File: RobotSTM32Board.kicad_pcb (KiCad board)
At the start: 2 copper layers, 70 x 82.5 mm, 19 parts, among them IC1 TB6612FNG, IC2 TB6612FNG, J1 MotorA, J2 MotorB, J3 MotorC, J4 MotorD, J5 EncoderA, J6 EncoderB, J7 EncoderC, J8 EncoderD, J9 ESTOP, U1 NUCLEO-F410RB, U2 BNO085, U3 ESP32-S3-WROOM-1

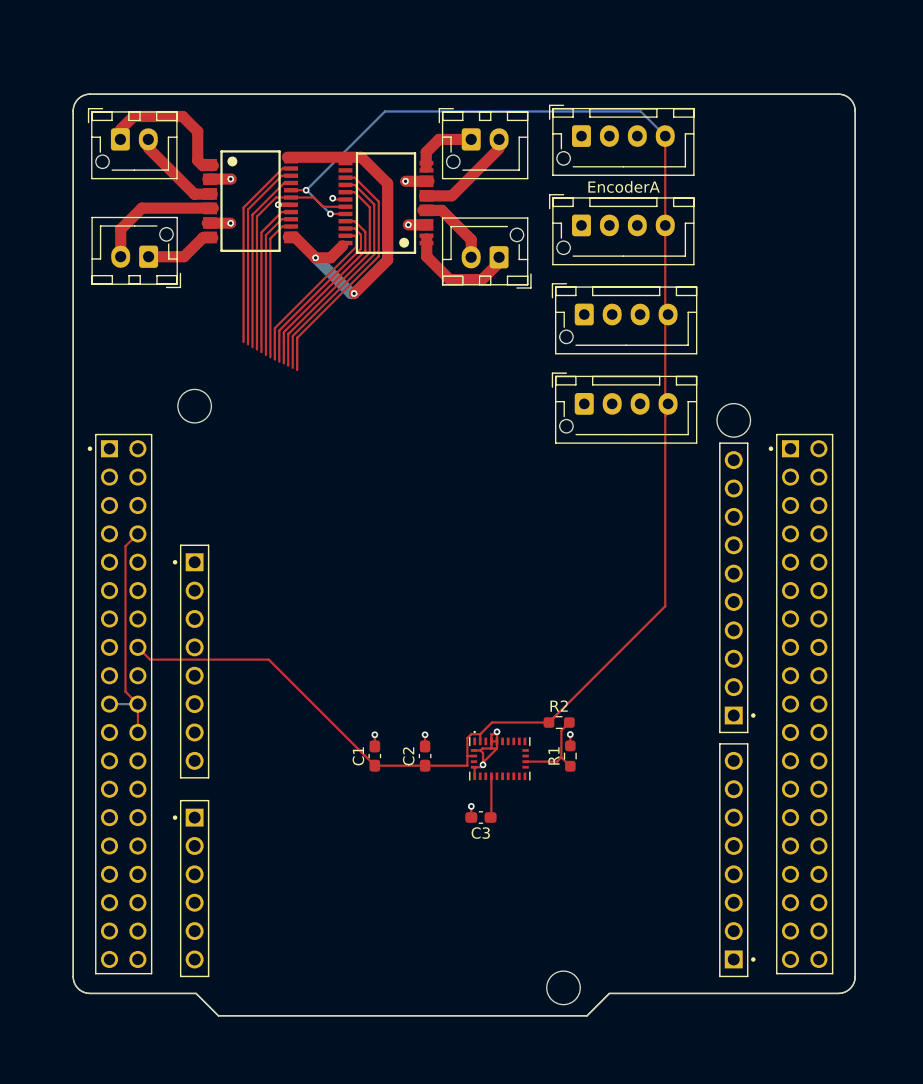
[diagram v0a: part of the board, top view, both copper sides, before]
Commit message: changed board to the one peter wilson gave us
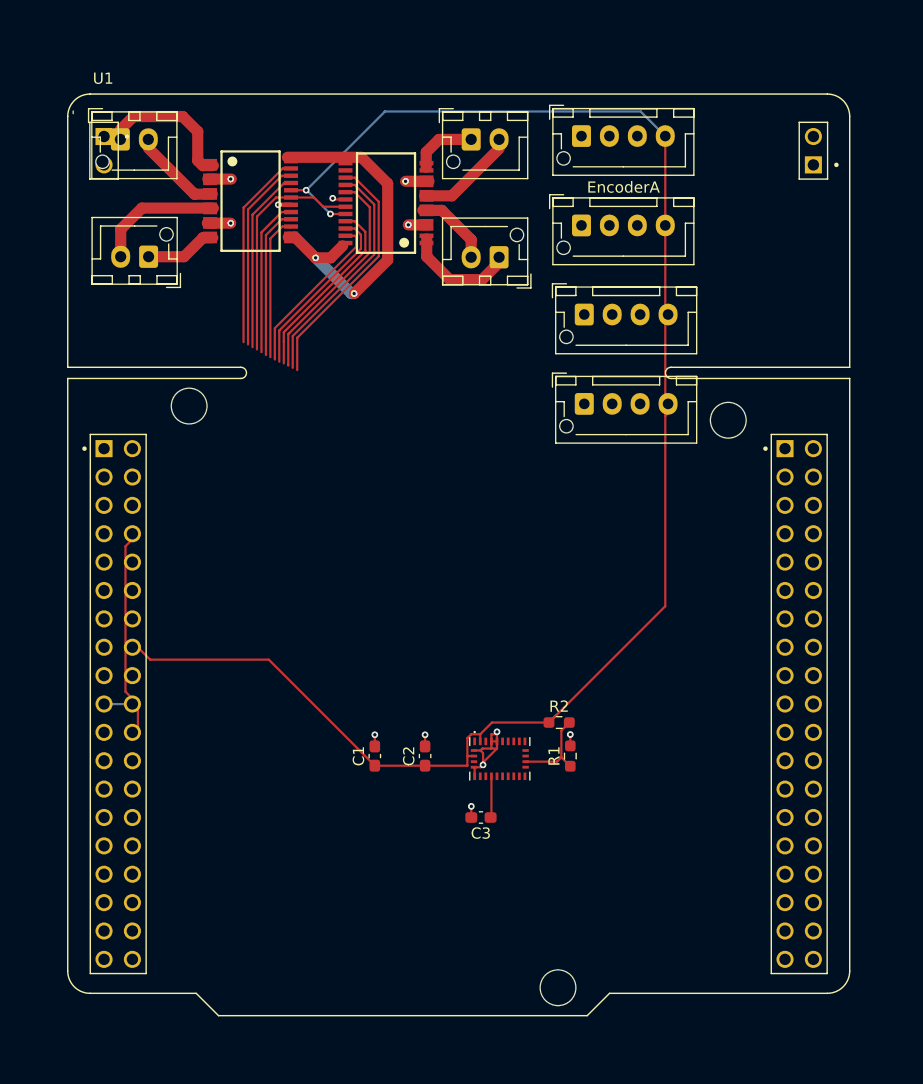
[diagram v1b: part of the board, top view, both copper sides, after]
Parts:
- U1: value NUCLEO-F410RB -> NUCLEO-F411RE; footprint NUCLEO-F410RB:ST_NUCLEO-F410RB -> NUCLEO-F411RE:BOARD_NUCLEO-F411RE
- moved U1 0.49 mm to (143.5, 93.5)
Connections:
- U1 pad CN7_10: (no net) -> unconnected-(U1A-NC_10_CN7-PadCN7_10)
- U1 pad CN7_11: (no net) -> unconnected-(U1A-NC_11-PadCN7_11)
- U1 pad CN7_16: 3V3 -> unconnected-(U1A-+3V3-PadCN7_16)
- U1 pad CN7_18: 5V -> unconnected-(U1A-+5V-PadCN7_18)
- U1 pad CN7_19: Net-(U1A-GND_CN7-PadCN7_19) -> unconnected-(U1A-GND_19-PadCN7_19)
- U1 pad CN7_20: Net-(U1A-GND_CN7-PadCN7_19) -> unconnected-(U1A-GND_20_CN7-PadCN7_20)
- U1 pad CN7_22: Net-(U1A-GND_CN7-PadCN7_19) -> unconnected-(U1A-GND_22-PadCN7_22)
- U1 pad CN7_26: (no net) -> unconnected-(U1A-NC_26-PadCN7_26)
- U1 pad CN7_8: Net-(U1A-GND_CN7-PadCN7_19) -> unconnected-(U1A-GND_8-PadCN7_8)
- U1 pad CN7_9: (no net) -> unconnected-(U1A-NC_9-PadCN7_9)
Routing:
- net Net-(U1A-GND_CN7-PadCN7_19): track 21.2 -> 0.00 mm
- net unconnected-(U1A-+5V-PadCN7_18): track 0.00 -> 18.7 mm
- net unconnected-(U1A-GND_20_CN7-PadCN7_20): track 0.00 -> 2.54 mm
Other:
- board outline removed

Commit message: pcb layout for the buck converters started
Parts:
- added C10: 10uF, Capacitor_SMD:C_0603_1608Metric, F.Cu at (149.8, 108.7)
- added C11: 1uF, Capacitor_SMD:C_0603_1608Metric, F.Cu at (142.1, 120.5)
- added C12: 220nF, Capacitor_SMD:C_0603_1608Metric, F.Cu at (144.7, 107.0)
- added C13: 10uF, Capacitor_SMD:C_0603_1608Metric, F.Cu at (132.4, 106.3)
- added C14: 27nf, Capacitor_SMD:C_0603_1608Metric, F.Cu at (132.4, 109.2)
- added C15: 100nF, Capacitor_SMD:C_0603_1608Metric, F.Cu at (130.6, 122.0)
- added C16: 1.2nF, Capacitor_SMD:C_0603_1608Metric, F.Cu at (133.4, 122.0)
- added C17: 180pF, Capacitor_SMD:C_0603_1608Metric, F.Cu at (130.7, 112.5)
- added C18: 1.2nF, Capacitor_SMD:C_0603_1608Metric, F.Cu at (132.4, 115.4)
- added C19: C_Small, Capacitor_SMD:C_0603_1608Metric, F.Cu at (153.7, 118.9)
- added C20: 220nF, Capacitor_SMD:C_0603_1608Metric, F.Cu at (152.2, 115.8)
- added C21: 120pF, Capacitor_SMD:C_0603_1608Metric, F.Cu at (157.6, 114.9)
- added C22: 10uF, Capacitor_SMD:C_0603_1608Metric, F.Cu at (152.9, 109.4)
- added C4: C_Small, Capacitor_SMD:C_0603_1608Metric, F.Cu at (118.2, 112.5)
- added C5: C_Small, Capacitor_SMD:C_0603_1608Metric, F.Cu at (119.1, 116.4)
- added C6: NC, Capacitor_SMD:C_0603_1608Metric, F.Cu at (161.4, 112.8)
- added C7: 1uF, Capacitor_SMD:C_0603_1608Metric, F.Cu at (158.3, 108.7)
- added C8: 0.1uF, Capacitor_SMD:C_0603_1608Metric, F.Cu at (162.9, 108.8)
- added C9: 22uf, Capacitor_SMD:C_0603_1608Metric, F.Cu at (166.4, 108.8)
- added D1: D_Zener_Small_Filled, Diode_SMD:D_0603_1608Metric, F.Cu at (139.3, 110.0)
- added J10: Qwiik1, Connector_JST:JST_SH_BM04B-SRSS-TB_1x04-1MP_P1.00mm_Vertical, F.Cu at (88.0, 44.0)
- added J11: Qwiik2, Connector_JST:JST_SH_BM04B-SRSS-TB_1x04-1MP_P1.00mm_Vertical, F.Cu at (88.0, 50.2)
- added J12: Qwiik3, Connector_JST:JST_SH_BM04B-SRSS-TB_1x04-1MP_P1.00mm_Vertical, F.Cu at (88.0, 56.5)
- added J13: Qwiik4, Connector_JST:JST_SH_BM04B-SRSS-TB_1x04-1MP_P1.00mm_Vertical, F.Cu at (88.0, 62.7)
- added J14: Qwiik5, Connector_JST:JST_SH_BM04B-SRSS-TB_1x04-1MP_P1.00mm_Vertical, F.Cu at (88.0, 69.0)
- added L1: L_Small, Inductor_SMD:L_0805_2012Metric, F.Cu at (121.0, 117.3)
- added L2: 1.5uH, Inductor_SMD:L_0805_2012Metric, F.Cu at (164.6, 109.0)
- added L3: 1uH, Inductor_SMD:L_0805_2012Metric, F.Cu at (150.4, 112.6)
- added Q1: NPN, Package_TO_SOT_SMD:SOT-23, F.Cu at (138.5, 121.8)
- added Q2: NMOS_Substrate, Package_TO_SOT_SMD:SOT-23, F.Cu at (145.6, 109.7)
- added Q3: NMOS_Substrate, Package_TO_SOT_SMD:SOT-23, F.Cu at (144.7, 114.4)
- added R10: 56.2k, Resistor_SMD:R_0603_1608Metric, F.Cu at (138.5, 107.6)
- added R11: 11k, Resistor_SMD:R_0603_1608Metric, F.Cu at (132.3, 118.2)
- added R12: 86.6k, Resistor_SMD:R_0603_1608Metric, F.Cu at (127.6, 122.0)
- added R13: 2.55k, Resistor_SMD:R_0603_1608Metric, F.Cu at (129.1, 115.4)
- added R14: 7.5k, Resistor_SMD:R_0603_1608Metric, F.Cu at (156.0, 118.2)
- added R15: 2.5k, Resistor_SMD:R_0603_1608Metric, F.Cu at (151.4, 118.2)
- added R16: 976, Resistor_SMD:R_0603_1608Metric, F.Cu at (148.8, 116.0)
- added R17: 20k, Resistor_SMD:R_0603_1608Metric, F.Cu at (154.5, 115.0)
- added R18: 2.23k, Resistor_SMD:R_0603_1608Metric, F.Cu at (127.5, 112.5)
- added R19: 225, Resistor_SMD:R_0603_1608Metric, F.Cu at (155.2, 112.8)
- added R3: R_Small, Resistor_SMD:R_0603_1608Metric, F.Cu at (121.3, 112.5)
- added R4: R_Small, Resistor_SMD:R_0603_1608Metric, F.Cu at (124.4, 112.5)
- added R5: R_Small, Resistor_SMD:R_0603_1608Metric, F.Cu at (123.6, 115.8)
- added R6: 130k, Resistor_SMD:R_0603_1608Metric, F.Cu at (168.1, 108.7)
- added R7: 20k, Resistor_SMD:R_0603_1608Metric, F.Cu at (167.2, 111.1)
- added R8: 100k, Resistor_SMD:R_0603_1608Metric, F.Cu at (159.3, 112.8)
- added R9: 2.21, Resistor_SMD:R_0603_1608Metric, F.Cu at (142.1, 118.7)
- added U4: TPS51386RJNR, TPS51386RJNR:VREG_TPS51386RJNR, F.Cu at (160.6, 109.2)
- added U5: LM27403SQ/NOPB, footprints:RTW24, F.Cu at (138.0, 115.2)
- U3: value ESP32-S3-WROOM-1 -> TPS564252DRLR; footprint RF_Module:ESP32-S3-WROOM-1 -> TPS564252DRLR:SOT50P160X60-6N
- moved U3 205.1 mm to (121.4, 114.5)
- moved C1 15.9 mm to (134.0, 95.8)
- moved C2 15.9 mm to (138.5, 95.8)
- moved C3 15.9 mm to (143.5, 101.3)
- moved R1 15.9 mm to (151.5, 95.8)
- moved R2 15.9 mm to (150.5, 92.8)
- moved U2 15.9 mm to (145.2, 96.0)
- moved IC1 4.93 mm to (129.8, 61.9)
- moved IC2 4.93 mm to (141.9, 62.0)
- moved J1 4.93 mm to (118.2, 56.4)
- moved J3 4.93 mm to (152.1, 66.9)
- moved J4 4.93 mm to (149.6, 56.4)
- moved J5 4.93 mm to (159.4, 56.0)
- moved J6 4.93 mm to (159.4, 64.0)
- moved J7 4.93 mm to (159.7, 72.0)
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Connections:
- U3 pad 1: Net-(U3-GND-Pad1) -> Vin
- U3 pad 2: unconnected-(U3-3V3-Pad2) -> Net-(U3-SW)
- U3 pad 3: unconnected-(U3-EN-Pad3) -> GND
- U3 pad 4: unconnected-(U3-IO4-Pad4) -> Net-(U3-PG)
- U3 pad 5: unconnected-(U3-IO5-Pad5) -> Vin
- U3 pad 6: unconnected-(U3-IO6-Pad6) -> Net-(U3-FB)
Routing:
- net Vin: track 0.00 -> 75.6 mm, vias 0 -> 3
- net 6V: track 32.3 -> 98.4 mm
- net GND: track 26.3 -> 87.5 mm, vias 12 -> 45
- net Net-(U5-FB): track 0.00 -> 36.6 mm, vias 0 -> 2
- net Net-(Q2-Bulk): track 0.00 -> 30.6 mm
- net Net-(D1-A): track 0.00 -> 24.5 mm, vias 0 -> 2
- net Net-(U5-CS-): track 0.00 -> 23.8 mm, vias 0 -> 2
- net Net-(U5-PGOOD): track 0.00 -> 23.7 mm, vias 0 -> 2
- net Net-(U5-CS+): track 0.00 -> 23.0 mm, vias 0 -> 2
- net unconnected-(U1A-+5V-PadCN7_18): track 18.7 -> 0.00 mm
- net Net-(Q1-B): track 0.00 -> 12.3 mm
- net Net-(U4-FB): track 0.00 -> 11.8 mm
- net Net-(U5-OTP): track 0.00 -> 11.8 mm
- net Net-(D1-K): track 0.00 -> 9.33 mm
- net Net-(Q2-G): track 0.00 -> 7.97 mm
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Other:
- board outline added: 70 x 82.5 mm

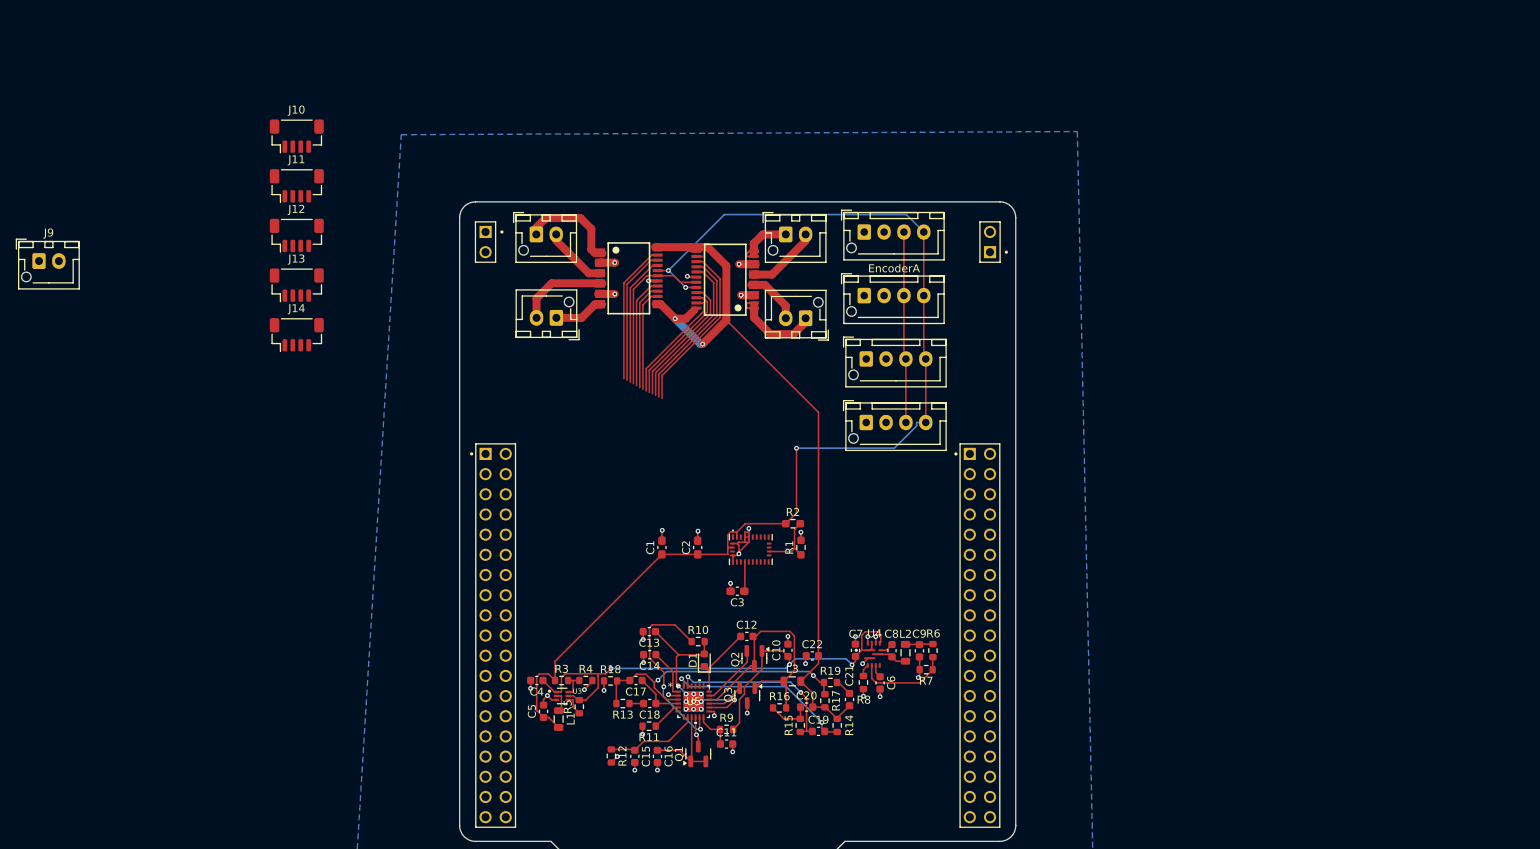
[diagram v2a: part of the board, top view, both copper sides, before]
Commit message: corrected buck converters
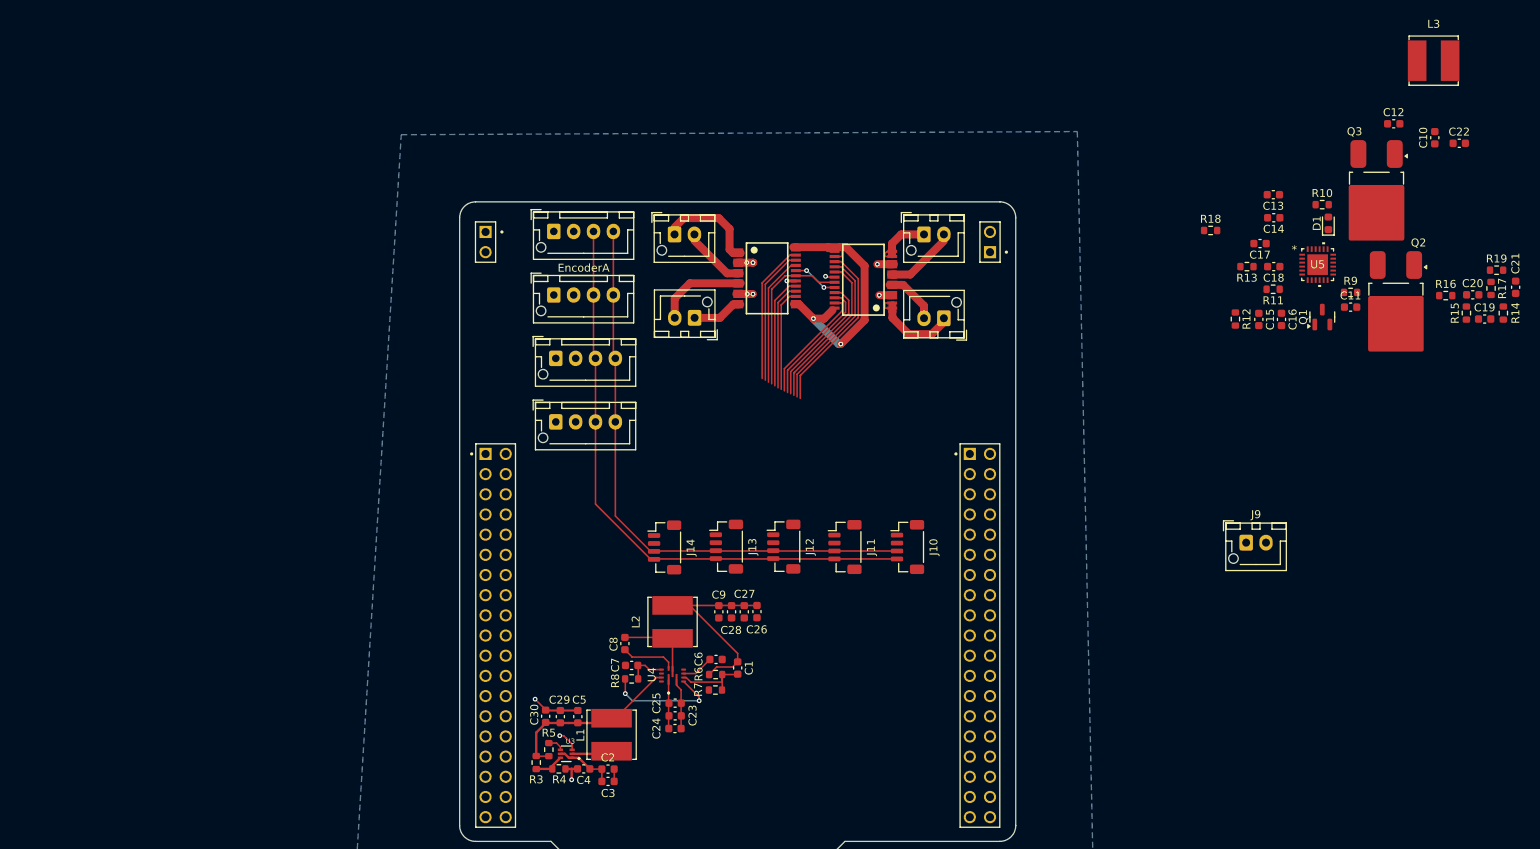
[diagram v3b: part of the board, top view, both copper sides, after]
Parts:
- removed R1: 0, Resistor_SMD:R_0603_1608Metric_Pad0.98x0.95mm_HandSolder
- removed R2: DNI, Resistor_SMD:R_0603_1608Metric_Pad0.98x0.95mm_HandSolder
- removed U2: BNO085, BNO085:IC_BNO085
- added C23: 10uF, Capacitor_SMD:C_0603_1608Metric, F.Cu at (135.6, 117.0)
- added C24: 10uF, Capacitor_SMD:C_0603_1608Metric, F.Cu at (135.6, 118.5)
- added C25: 0.1uF, Capacitor_SMD:C_0603_1608Metric, F.Cu at (135.6, 115.3)
- added C26: 22uf, Capacitor_SMD:C_0603_1608Metric, F.Cu at (145.9, 103.8)
- added C27: 22uf, Capacitor_SMD:C_0603_1608Metric, F.Cu at (144.3, 103.8)
- added C28: 22uf, Capacitor_SMD:C_0603_1608Metric, F.Cu at (142.7, 103.8)
- added C29: 22uF, Capacitor_SMD:C_0603_1608Metric, F.Cu at (121.2, 117.0)
- added C30: 100nF, Capacitor_SMD:C_0603_1608Metric, F.Cu at (119.3, 117.0)
- C1: value 0.1uF -> 22pf; footprint Capacitor_SMD:C_0603_1608Metric_Pad1.08x0.95mm_HandSolder -> Capacitor_SMD:C_0603_1608Metric
- C2: value 0.1uF -> 10uF; footprint Capacitor_SMD:C_0603_1608Metric_Pad1.08x0.95mm_HandSolder -> Capacitor_SMD:C_0603_1608Metric
- C3: value 0.1uF -> 100nF; footprint Capacitor_SMD:C_0603_1608Metric_Pad1.08x0.95mm_HandSolder -> Capacitor_SMD:C_0603_1608Metric
- C4: value C_Small -> 10uF
- C5: value C_Small -> 22uF
- L1: value L_Small -> 3.3uH; footprint Inductor_SMD:L_0805_2012Metric -> Inductor_SMD:L_Bourns_SRN6045TA
- L2, L3: footprint Inductor_SMD:L_0805_2012Metric -> Inductor_SMD:L_Bourns_SRN6045TA
- Q2, Q3: footprint Package_TO_SOT_SMD:SOT-23 -> Package_TO_SOT_SMD:TO-252-2_TabPin1
- R3: value R_Small -> 45k
- R4, R5: value R_Small -> 10k
- R6: value 130k -> 150k
- moved J9 156.0 mm to (207.5, 95.2)
- moved L3 112.3 mm to (231.1, 34.5)
- moved C10 103.9 mm to (231.2, 44.2)
- moved C12 103.9 mm to (226.1, 42.4)
- moved C22 103.9 mm to (234.3, 44.9)
- moved Q3 101.1 mm to (223.9, 51.6)
- moved C21 98.6 mm to (241.4, 63.0)
- moved C19 98.6 mm to (237.5, 67.0)
- moved C20 98.6 mm to (236.0, 64.0)
- moved R14 98.6 mm to (239.9, 66.2)
- moved R15 98.6 mm to (235.2, 66.2)
- moved R16 98.6 mm to (232.6, 64.0)
- moved R17 98.6 mm to (238.3, 63.1)
- moved R19 98.6 mm to (239.0, 60.9)
- moved C11 95.9 mm to (220.7, 65.5)
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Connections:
- C1 pad 1: 3V3 -> 5V
- C1 pad 2: GND -> Net-(U4-FB)
- C2 pad 1: 3V3 -> Vin
- C3 pad 1: Net-(U2-CAP) -> Vin
- C7 pad 1: Vin -> Net-(U4-VCC)
- J10 pad 1: unconnected-(J10-Pin_1-Pad1) -> SCL
- J10 pad 2: unconnected-(J10-Pin_2-Pad2) -> SDA
- J10 pad 3: unconnected-(J10-Pin_3-Pad3) -> 3V3
- J10 pad 4: unconnected-(J10-Pin_4-Pad4) -> GND
- J11 pad 1: unconnected-(J11-Pin_1-Pad1) -> SCL
- J11 pad 2: unconnected-(J11-Pin_2-Pad2) -> SDA
- J11 pad 3: unconnected-(J11-Pin_3-Pad3) -> 3V3
- J11 pad 4: unconnected-(J11-Pin_4-Pad4) -> GND
- J12 pad 1: unconnected-(J12-Pin_1-Pad1) -> SCL
- J12 pad 2: unconnected-(J12-Pin_2-Pad2) -> SDA
- J12 pad 3: unconnected-(J12-Pin_3-Pad3) -> 3V3
- J12 pad 4: unconnected-(J12-Pin_4-Pad4) -> GND
- J13 pad 1: unconnected-(J13-Pin_1-Pad1) -> SCL
- J13 pad 2: unconnected-(J13-Pin_2-Pad2) -> SDA
- J13 pad 3: unconnected-(J13-Pin_3-Pad3) -> 3V3
- J13 pad 4: unconnected-(J13-Pin_4-Pad4) -> GND
- J14 pad 1: unconnected-(J14-Pin_1-Pad1) -> SCL
- J14 pad 2: unconnected-(J14-Pin_2-Pad2) -> SDA
- J14 pad 3: unconnected-(J14-Pin_3-Pad3) -> 3V3
- J14 pad 4: unconnected-(J14-Pin_4-Pad4) -> GND
- R5 pad 2: Vin -> 3V3
- R8 pad 2: GND -> Net-(U4-VCC)
- U1 pad CN10_1: (no net) -> unconnected-(U1B-PC9-PadCN10_1)
- U1 pad CN10_10: (no net) -> unconnected-(U1B-NC_10_CN10-PadCN10_10)
- U1 pad CN10_11: (no net) -> unconnected-(U1B-PA5-PadCN10_11)
- U1 pad CN10_12: (no net) -> unconnected-(U1B-PA12-PadCN10_12)
- U1 pad CN10_13: (no net) -> unconnected-(U1B-PA6-PadCN10_13)
- U1 pad CN10_14: (no net) -> unconnected-(U1B-PA11-PadCN10_14)
- U1 pad CN10_15: (no net) -> unconnected-(U1B-PA7-PadCN10_15)
- U1 pad CN10_16: (no net) -> unconnected-(U1B-PB12-PadCN10_16)
- U1 pad CN10_17: (no net) -> unconnected-(U1B-PB6-PadCN10_17)
- U1 pad CN10_18: (no net) -> unconnected-(U1B-NC_18-PadCN10_18)
- U1 pad CN10_19: (no net) -> unconnected-(U1B-PC7-PadCN10_19)
- U1 pad CN10_2: (no net) -> unconnected-(U1B-PC8-PadCN10_2)
- U1 pad CN10_20: (no net) -> unconnected-(U1B-GND_20_CN10-PadCN10_20)
- U1 pad CN10_21: (no net) -> unconnected-(U1B-PA9-PadCN10_21)
- U1 pad CN10_22: (no net) -> unconnected-(U1B-PB2-PadCN10_22)
- U1 pad CN10_23: (no net) -> unconnected-(U1B-PA8-PadCN10_23)
- U1 pad CN10_24: (no net) -> unconnected-(U1B-PB1-PadCN10_24)
- U1 pad CN10_25: (no net) -> unconnected-(U1B-PB10-PadCN10_25)
- U1 pad CN10_26: (no net) -> unconnected-(U1B-PB15-PadCN10_26)
- U1 pad CN10_27: (no net) -> unconnected-(U1B-PB4-PadCN10_27)
- U1 pad CN10_28: (no net) -> unconnected-(U1B-PB14-PadCN10_28)
- U1 pad CN10_29: (no net) -> unconnected-(U1B-PB5-PadCN10_29)
- U1 pad CN10_3: (no net) -> unconnected-(U1B-PB8-PadCN10_3)
- U1 pad CN10_30: (no net) -> unconnected-(U1B-PB13-PadCN10_30)
- U1 pad CN10_31: (no net) -> unconnected-(U1B-PB3-PadCN10_31)
- U1 pad CN10_32: (no net) -> unconnected-(U1B-AGND-PadCN10_32)
- U1 pad CN10_33: (no net) -> unconnected-(U1B-PA10-PadCN10_33)
- U1 pad CN10_34: (no net) -> unconnected-(U1B-PC4-PadCN10_34)
- U1 pad CN10_35: (no net) -> unconnected-(U1B-PA2-PadCN10_35)
- U1 pad CN10_36: (no net) -> unconnected-(U1B-NC_36-PadCN10_36)
- U1 pad CN10_37: (no net) -> unconnected-(U1B-PA3-PadCN10_37)
- U1 pad CN10_38: (no net) -> unconnected-(U1B-NC_38-PadCN10_38)
- U1 pad CN10_4: (no net) -> unconnected-(U1B-PC6-PadCN10_4)
- U1 pad CN10_5: (no net) -> unconnected-(U1B-PB9-PadCN10_5)
- U1 pad CN10_6: (no net) -> unconnected-(U1B-PC5-PadCN10_6)
- U1 pad CN10_7: (no net) -> unconnected-(U1B-AVDD-PadCN10_7)
- U1 pad CN10_8: (no net) -> unconnected-(U1B-U5V-PadCN10_8)
- U1 pad CN10_9: (no net) -> unconnected-(U1B-GND_9-PadCN10_9)
- U1 pad CN11_1: (no net) -> unconnected-(U1-PadCN11_1)
- U1 pad CN11_2: (no net) -> unconnected-(U1-PadCN11_2)
- U1 pad CN12_1: (no net) -> unconnected-(U1-PadCN12_1)
- U1 pad CN12_2: (no net) -> unconnected-(U1-PadCN12_2)
- U1 pad CN7_1: unconnected-(U1A-PC10-PadCN7_1) -> MotorPWMA
- U1 pad CN7_13: unconnected-(U1A-PA13-PadCN7_13) -> MotorBCW
- U1 pad CN7_2: unconnected-(U1A-PC11-PadCN7_2) -> MotorACCW
- U1 pad CN7_3: unconnected-(U1A-PC12-PadCN7_3) -> MotorACW
- U1 pad CN7_4: unconnected-(U1A-PD2-PadCN7_4) -> MotorBCCW
- U4 pad 11: Vin -> 3V3
- U4 pad 9: Vin -> Net-(U4-VCC)
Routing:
- net Vin: track 75.6 -> 13.7 mm, vias 3 -> 0
- net 6V: track 98.4 -> 37.4 mm
- net 3V3: track 147.0 -> 102.5 mm, vias 3 -> 2
- net Net-(U5-FB): track 36.6 -> 0.00 mm, vias 2 -> 0
- net Net-(Q2-Bulk): track 30.6 -> 0.00 mm
- net GND: track 87.5 -> 113.3 mm, vias 45 -> 11
- net Net-(D1-A): track 24.5 -> 0.00 mm, vias 2 -> 0
- net Net-(U5-CS-): track 23.8 -> 0.00 mm, vias 2 -> 0
- net Net-(U5-PGOOD): track 23.7 -> 0.00 mm, vias 2 -> 0
- net 5V: track 3.50 -> 26.8 mm
- net Net-(U5-CS+): track 23.0 -> 0.00 mm, vias 2 -> 0
- net Net-(U4-PG): track 1.55 -> 14.8 mm, vias 0 -> 2
- net Net-(Q1-B): track 12.3 -> 0.00 mm
- net Net-(U5-OTP): track 11.8 -> 0.00 mm
- net Net-(D1-K): track 9.33 -> 0.00 mm
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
